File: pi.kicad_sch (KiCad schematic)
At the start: 23 parts, among them J5 Conn_01x12-Socket, J6 Conn_01x12-Socket, J7 Conn_01x12-Header, J8 Conn_01x12-Header, M1 Fan_4pin, M2 Fan_4pin, U30 T-Display-S3, U32 EMC2302-1, U33 TXU0102-DCU, U37 TMP1075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

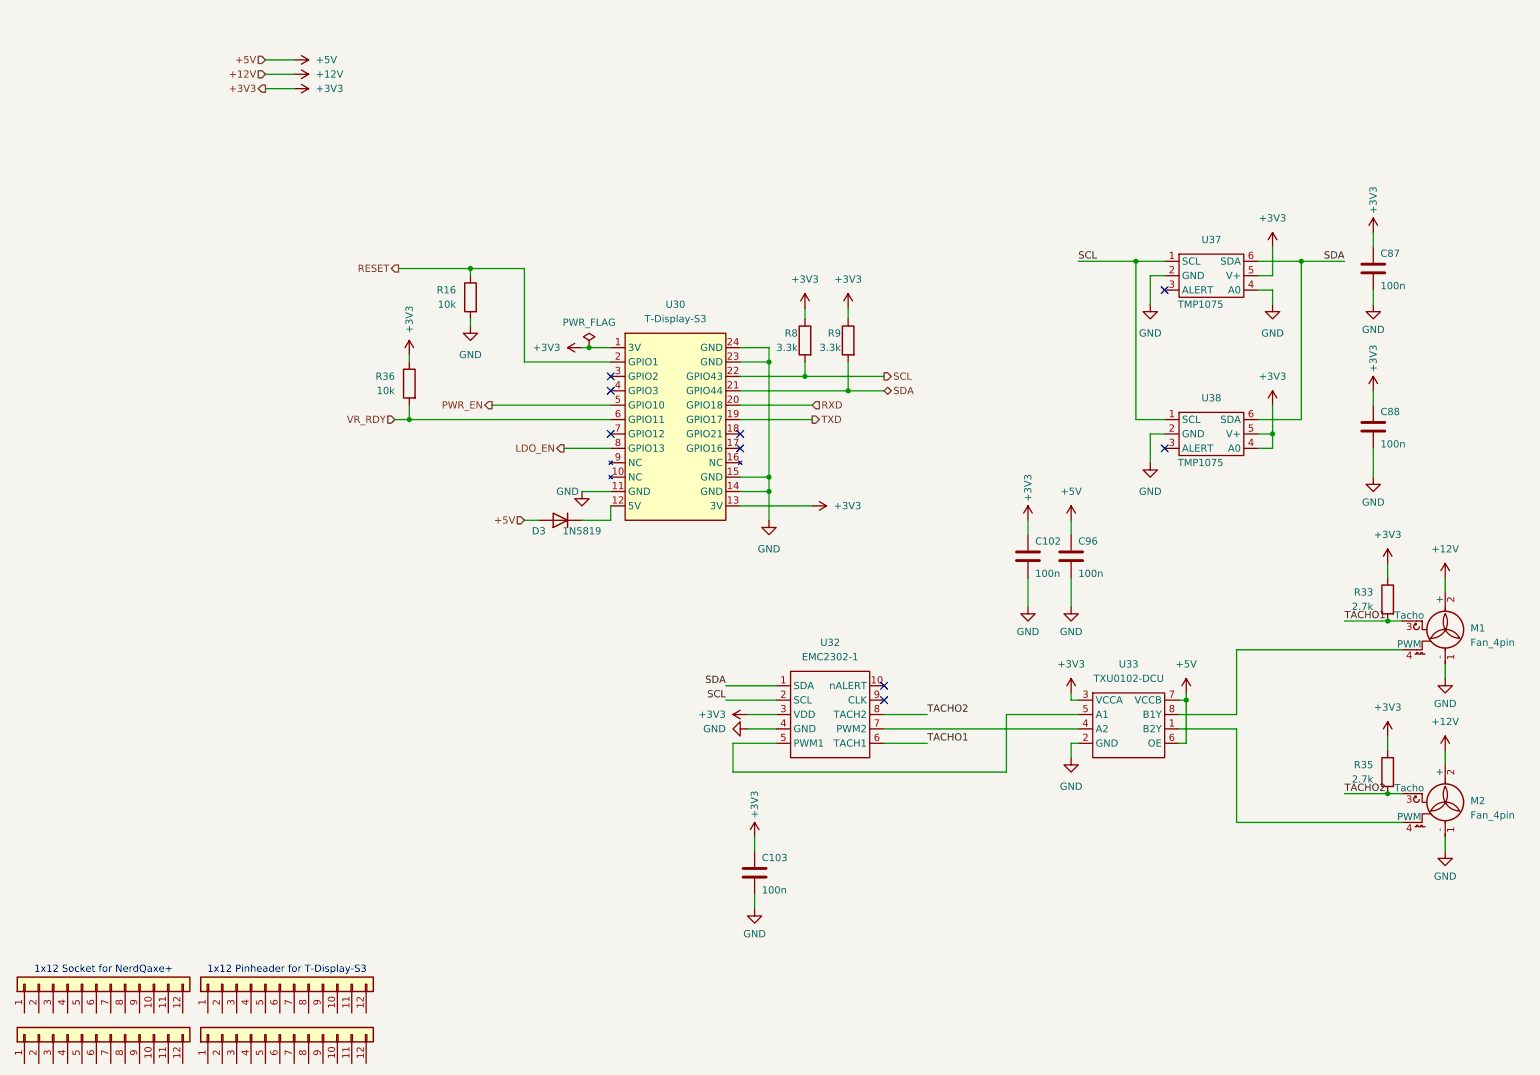
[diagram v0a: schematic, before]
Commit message: updated power stage placements
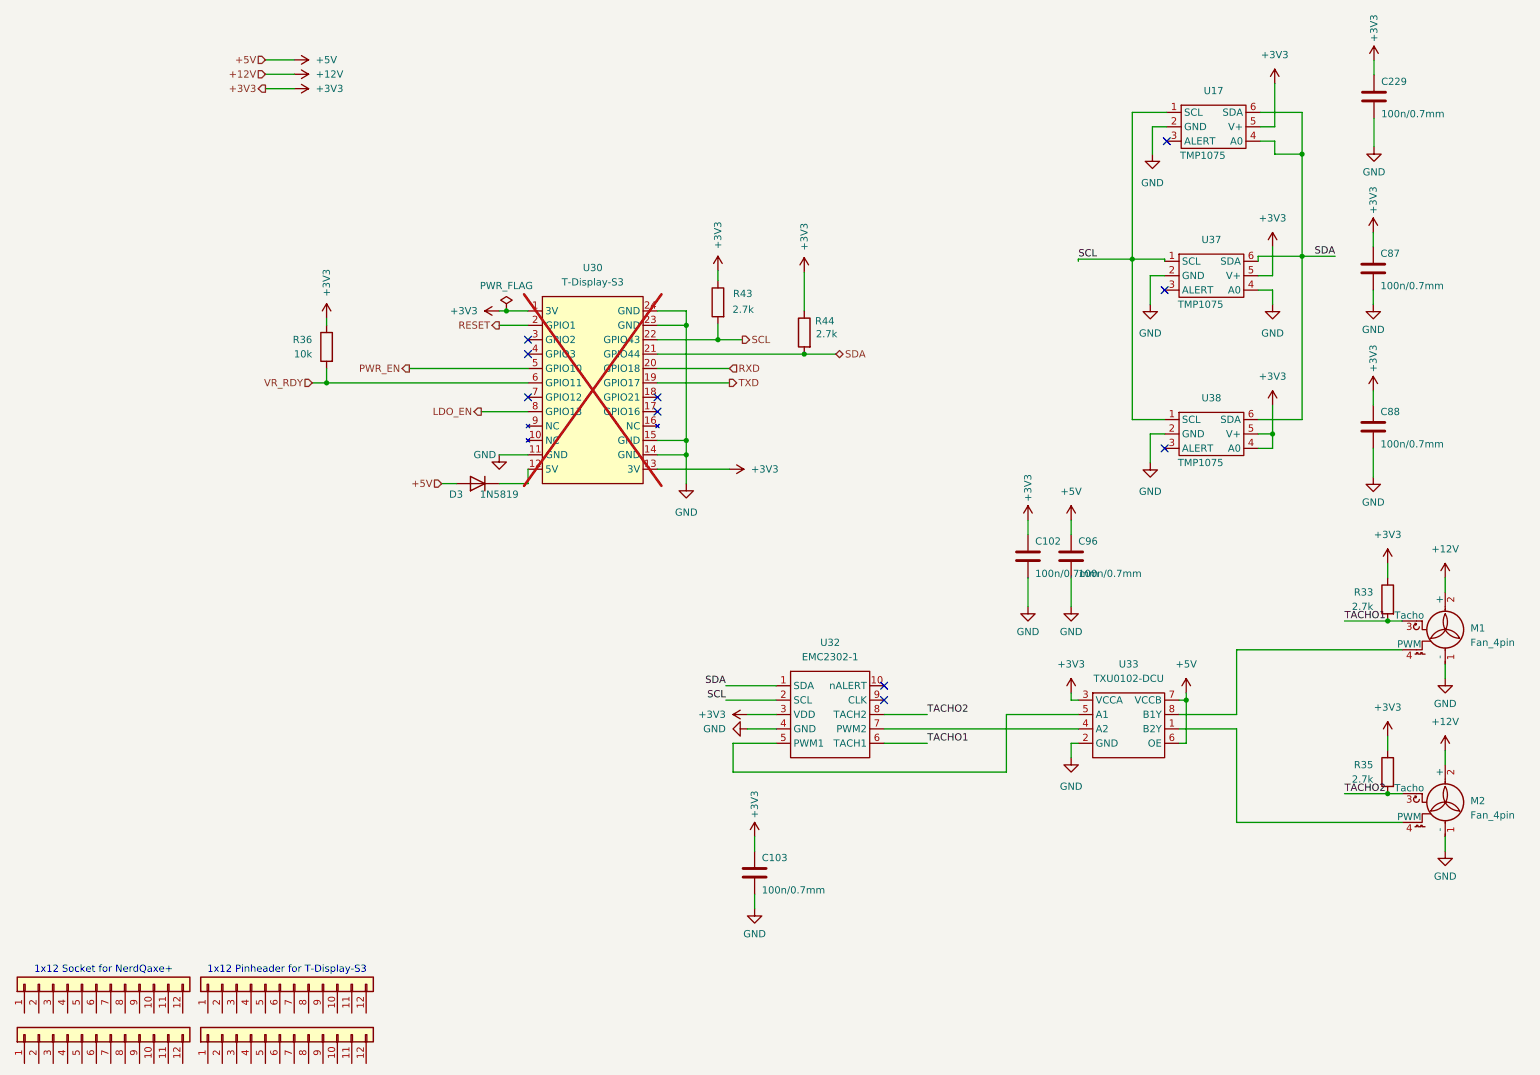
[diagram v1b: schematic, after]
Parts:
- removed R16: 10k, Resistor_SMD:R_0805_2012Metric, symbol Device:R
- removed R8, R9: 3.3k, Resistor_SMD:R_0805_2012Metric, symbol Device:R
- added C229: 100n/0.7mm, Capacitor_SMD:C_0805_2012Metric, symbol Device:C
- added R43, R44: 2.7k, Resistor_SMD:R_0805_2012Metric, symbol Device:R
- added U17: TMP1075, myfootprints:TMP1075-DRL, symbol mylib7:TMP1075-DRL-SOT563
- C102, C103, C87, C88, C96: value 100n -> 100n/0.7mm; Manufacturer C0805C104K5RACTU -> AC0805KRX7R9BB104; OrderNr 399-C0805C104K5RACTUCT-ND -> 311-3037-1-ND; temp-coefficient X7R -> (none)
- U30: Manufacturer T-Display S3 [H577] -> (none); OrderNr T-Display S3 [H577] -> (none); now not fitted
- U38: footprint myfootprints:TMP1075-DRL -> Nerd8:TMP1075-DRL
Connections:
- net +3V3: now also C229.1, R43.1, R44.1, U17.5 (V+)
- net GND: now also C229.2, U17.2 (GND)
- net SCL: now also R43.2, U17.1 (SCL)
- net SDA: now also R44.2, U17.4 (A0), U17.6 (SDA)
- no-connect marks 9 -> 10
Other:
- moved on the sheet: D3, R36
